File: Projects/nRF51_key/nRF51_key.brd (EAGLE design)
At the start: 45.7 x 12 mm, 14 parts, among them IC1 FT230XQ, J1 47571-0001, X1 USBPCB

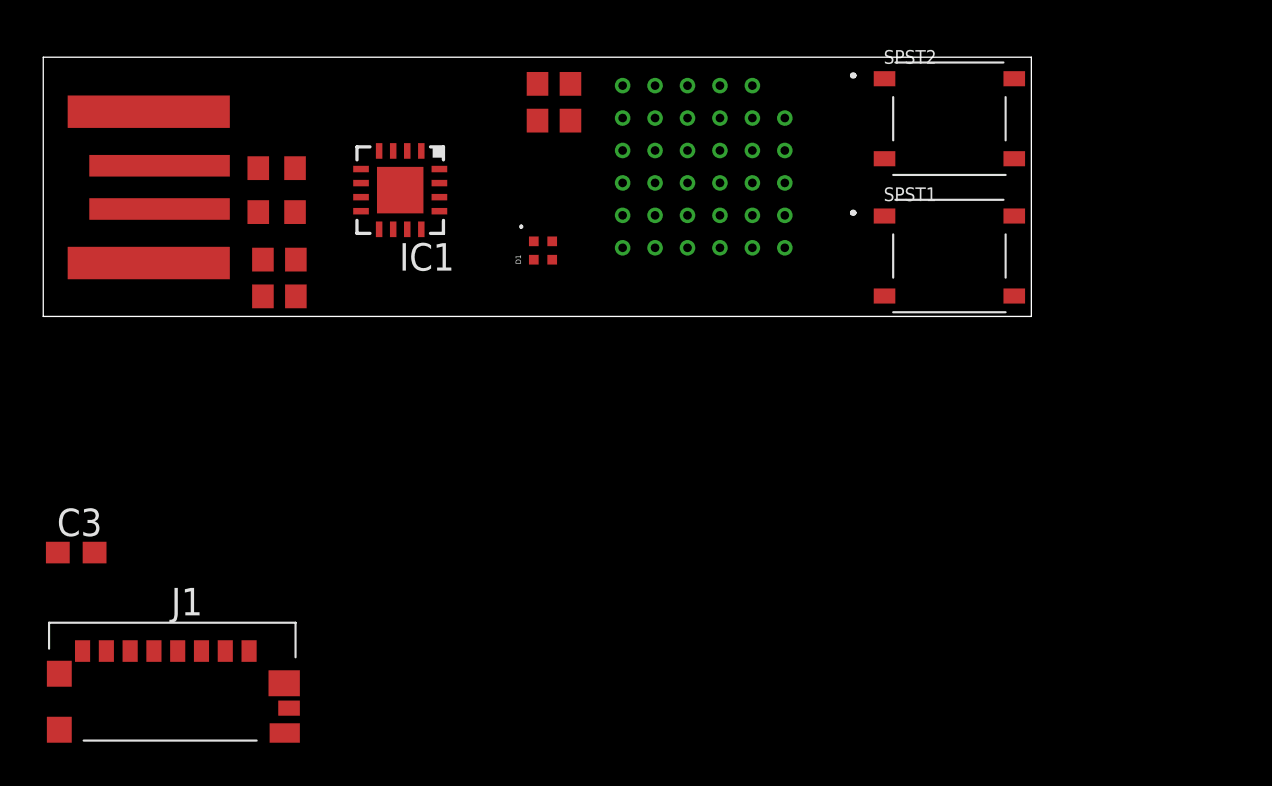
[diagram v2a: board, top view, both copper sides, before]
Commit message: Corrected SD card library
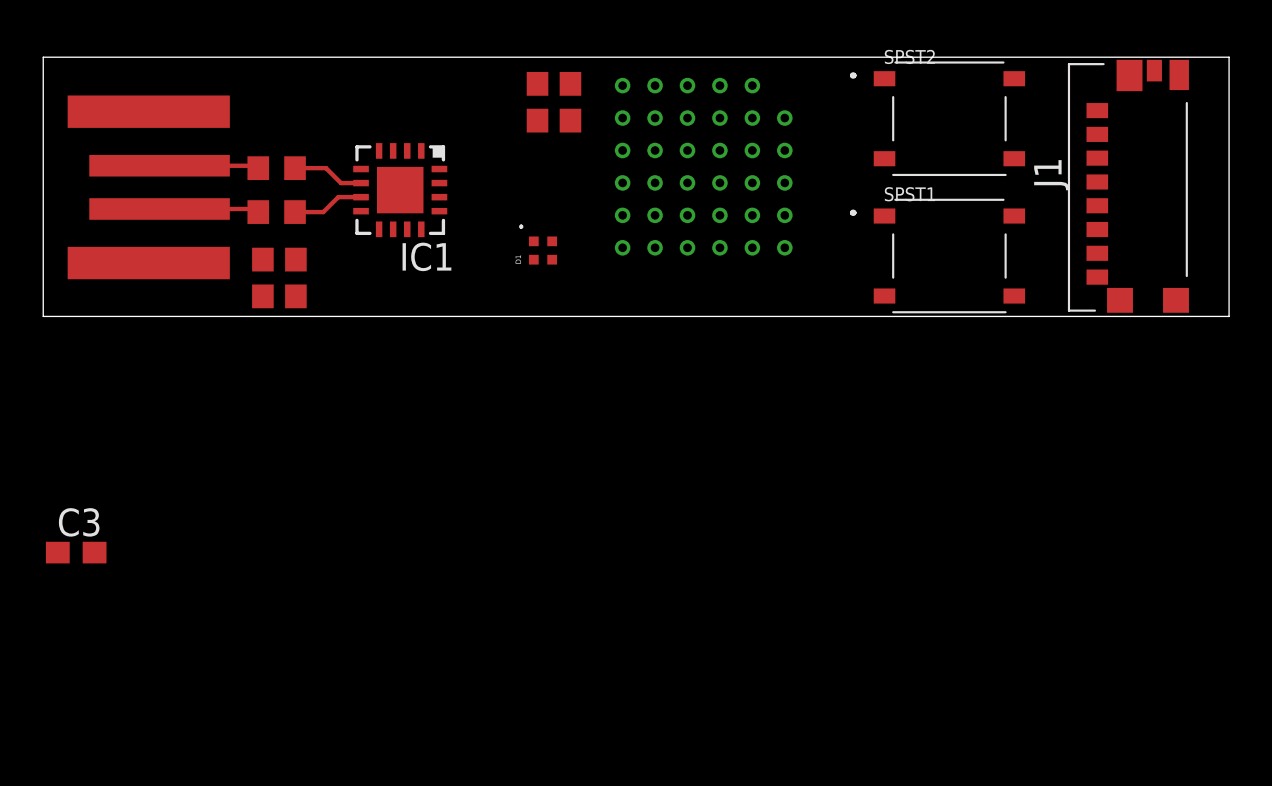
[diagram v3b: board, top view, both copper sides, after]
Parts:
- moved J1 49.8 mm to (50.2, 14.0), turned to 90 degrees
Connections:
- net CLK: now also J1.25; no longer J1.5
- net CS: now also J1.22; no longer J1.2
- net GND: now also J1.26; no longer J1.6
- net MISO: now also J1.27; no longer J1.7
- net MOSI: now also J1.23; no longer J1.3
- net SWDCLK: now also J1.21; no longer J1.8
- net SWDIO: now also J1.28; no longer J1.1
- net VDD: now also J1.24; no longer J1.4
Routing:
- net USBDM: track 0.00 -> 4.62 mm
- net USBDP: track 0.00 -> 4.61 mm
- net IC1_USBDM: track 0.00 -> 3.34 mm
- net IC1_USBDP: track 0.00 -> 3.34 mm
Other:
- board size 45.7 x 12 mm -> 54.8 x 12 mm
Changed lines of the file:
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@@
 <board>
 <plain>
-<wire x1="0" y1="8.001" x2="45.7" y2="8.001" width="0" layer="20"/>
-<wire x1="45.7" y1="8.001" x2="45.7" y2="19.99" width="0" layer="20"/>
-<wire x1="45.7" y1="19.99" x2="0" y2="19.99" width="0" layer="20"/>
+<wire x1="0" y1="8.001" x2="54.844" y2="8.001" width="0" layer="20"/>
+<wire x1="54.844" y1="8.001" x2="54.844" y2="19.99" width="0" layer="20"/>
+<wire x1="54.844" y1="19.99" x2="0" y2="19.99" width="0" layer="20"/>
 <wire x1="0" y1="19.99" x2="0" y2="8.001" width="0" layer="20"/>
 </plain>
@@
 <attribute name="VALUE" x="9.906" y="12.827" size="1.27" layer="27"/>
 </element>
-<element name="J1" library="SD_Card" package="47571-0001" value="47571-0001" x="5.969" y="-8.89" smashed="yes">
-<attribute name="NAME" x="6.645" y="-5.189" size="1.27" layer="25" align="center"/>
-<attribute name="VALUE" x="5.883" y="-12.555" size="1.27" layer="27" align="center"/>
+<element name="J1" library="SD_Card" package="47571-0001" value="47571-0001" x="50.165" y="13.97" smashed="yes" rot="R90">
+<attribute name="NAME" x="46.464" y="14.646" size="1.27" layer="25" rot="R90" align="center"/>
+<attribute name="VALUE" x="53.83" y="13.884" size="1.27" layer="27" rot="R90" align="center"/>
 </element>
 </elements>
@@
 <contactref element="C2" pad="2"/>
 <contactref element="C1" pad="2"/>
-<contactref element="J1" pad="6"/>
+<contactref element="J1" pad="26"/>
 <contactref element="J1" pad="13"/>
 <contactref element="J1" pad="11"/>
@@
 <contactref element="J1" pad="9"/>
 <contactref element="J1" pad="10"/>
+<wire x1="51.39" y1="19.37" x2="52.54" y2="19.17" width="0" layer="19" extent="1-1"/>
+<wire x1="50.24" y1="19.145" x2="51.39" y2="19.37" width="0" layer="19" extent="1-1"/>
+<wire x1="44.91" y1="15.295" x2="50.24" y2="19.145" width="0" layer="19" extent="1-1"/>
+<wire x1="48.75" y1="12.02" x2="44.91" y2="15.295" width="0" layer="19" extent="1-1"/>
+<wire x1="49.8" y1="8.745" x2="48.75" y2="12.02" width="0" layer="19" extent="1-1"/>
+<wire x1="52.39" y1="8.745" x2="49.8" y2="8.745" width="0" layer="19" extent="1-1"/>
+<wire x1="44.91" y1="8.945" x2="49.8" y2="8.745" width="0" layer="19" extent="1-1"/>
 <wire x1="38.91" y1="15.295" x2="44.91" y2="15.295" width="0" layer="19" extent="1-1"/>
-<wire x1="44.91" y1="8.945" x2="44.91" y2="15.295" width="0" layer="19" extent="1-1"/>
 <wire x1="38.91" y1="8.945" x2="44.91" y2="8.945" width="0" layer="19" extent="1-1"/>
 <wire x1="32.797" y1="18.676" x2="38.91" y2="15.295" width="0" layer="19" extent="1-1"/>
@@
 <wire x1="4.88" y1="17.47" x2="10.16" y2="8.929" width="0" layer="19" extent="1-1"/>
 <wire x1="2.374" y1="-2.921" x2="10.16" y2="8.929" width="0" layer="19" extent="1-1"/>
-<wire x1="0.744" y1="-8.525" x2="2.374" y2="-2.921" width="0" layer="19" extent="1-1"/>
-<wire x1="0.744" y1="-11.115" x2="0.744" y2="-8.525" width="0" layer="19" extent="1-1"/>
-<wire x1="7.319" y1="-7.475" x2="0.744" y2="-8.525" width="0" layer="19" extent="1-1"/>
-<wire x1="11.144" y1="-8.965" x2="7.319" y2="-7.475" width="0" layer="19" extent="1-1"/>
-<wire x1="11.369" y1="-10.115" x2="11.144" y2="-8.965" width="0" layer="19" extent="1-1"/>
-<wire x1="11.169" y1="-11.265" x2="11.369" y2="-10.115" width="0" layer="19" extent="1-1"/>
 </signal>
 <signal name="USBDP">
 <contactref element="X1" pad="USB_P"/>
 <contactref element="R2" pad="1"/>
-<wire x1="5.38" y1="14.97" x2="9.945" y2="14.859" width="0" layer="19" extent="1-1"/>
+<wire x1="5.38" y1="14.97" x2="9.834" y2="14.97" width="0.2032" layer="1"/>
+<wire x1="9.834" y1="14.97" x2="9.945" y2="14.859" width="0.2032" layer="1"/>
 </signal>
 <signal name="USBDM">
 <contactref element="X1" pad="USB_M"/>
 <contactref element="R1" pad="1"/>
-<wire x1="5.38" y1="12.97" x2="9.945" y2="12.827" width="0" layer="19" extent="1-1"/>
+<wire x1="5.38" y1="12.97" x2="9.802" y2="12.97" width="0.2032" layer="1"/>
+<wire x1="9.802" y1="12.97" x2="9.945" y2="12.827" width="0.2032" layer="1"/>
 </signal>
 <signal name="VBUS">
@@
 <contactref element="IC1" pad="9"/>
 <contactref element="IC1" pad="1"/>
-<contactref element="J1" pad="4"/>
-<wire x1="28.297" y1="15.676" x2="28.297" y2="17.176" width="0" layer="19" extent="1-1"/>
+<contactref element="J1" pad="24"/>
+<wire x1="28.297" y1="15.676" x2="48.75" y2="14.22" width="0" layer="19" extent="1-1"/>
+<wire x1="28.297" y1="17.176" x2="28.297" y2="15.676" width="0" layer="19" extent="1-1"/>
 <wire x1="26.797" y1="17.176" x2="28.297" y2="17.176" width="0" layer="19" extent="1-1"/>
 <wire x1="26.797" y1="15.676" x2="28.297" y2="15.676" width="0" layer="19" extent="1-1"/>
@@
 <wire x1="15.535" y1="12.0305" x2="14.6975" y2="12.868" width="0" layer="19" extent="1-1"/>
 <wire x1="22.689" y1="11.474" x2="22.86" y2="17.057" width="0" layer="19" extent="1-1"/>
-<wire x1="5.119" y1="-7.475" x2="15.535" y2="12.0305" width="0" layer="19" extent="1-1"/>
 </signal>
 <signal name="BTN1">
@@
 <contactref element="IC1" pad="7"/>
 <contactref element="R1" pad="2"/>
-<wire x1="11.645" y1="12.827" x2="14.6975" y2="13.518" width="0" layer="19" extent="1-1"/>
+<wire x1="11.645" y1="12.827" x2="12.954" y2="12.827" width="0.2032" layer="1"/>
+<wire x1="13.645" y1="13.518" x2="14.6975" y2="13.518" width="0.2032" layer="1"/>
+<wire x1="12.954" y1="12.827" x2="13.645" y2="13.518" width="0.2032" layer="1"/>
 </signal>
 <signal name="IC1_USBDP">
 <contactref element="IC1" pad="6"/>
 <contactref element="R2" pad="2"/>
-<wire x1="11.645" y1="14.859" x2="14.6975" y2="14.168" width="0" layer="19" extent="1-1"/>
+<wire x1="11.645" y1="14.859" x2="13.081" y2="14.859" width="0.2032" layer="1"/>
+<wire x1="13.772" y1="14.168" x2="14.6975" y2="14.168" width="0.2032" layer="1"/>
+<wire x1="13.081" y1="14.859" x2="13.772" y2="14.168" width="0.2032" layer="1"/>
 </signal>
 <signal name="MISO">
-<contactref element="J1" pad="7"/>
+<contactref element="J1" pad="27"/>
 </signal>
 <signal name="CLK">
-<contactref element="J1" pad="5"/>
+<contactref element="J1" pad="25"/>
 </signal>
 <signal name="MOSI">
-<contactref element="J1" pad="3"/>
+<contactref element="J1" pad="23"/>
 </signal>
 <signal name="CS">
-<contactref element="J1" pad="2"/>
+<contactref element="J1" pad="22"/>
 </signal>
 <signal name="SWDIO">
 <contactref element="U$1" pad="SWDIO"/>
-<contactref element="J1" pad="1"/>
-<wire x1="1.819" y1="-7.475" x2="34.297" y2="17.176" width="0" layer="19" extent="1-1"/>
+<contactref element="J1" pad="28"/>
+<wire x1="34.297" y1="17.176" x2="48.75" y2="9.82" width="0" layer="19" extent="1-1"/>
 </signal>
 <signal name="SWDCLK">
 <contactref element="U$1" pad="SWDCLK"/>
-<contactref element="J1" pad="8"/>
-<wire x1="9.519" y1="-7.475" x2="34.297" y2="15.676" width="0" layer="19" extent="1-1"/>
+<contactref element="J1" pad="21"/>
+<wire x1="34.297" y1="15.676" x2="48.75" y2="17.52" width="0" layer="19" extent="1-1"/>
 </signal>
 </signals>

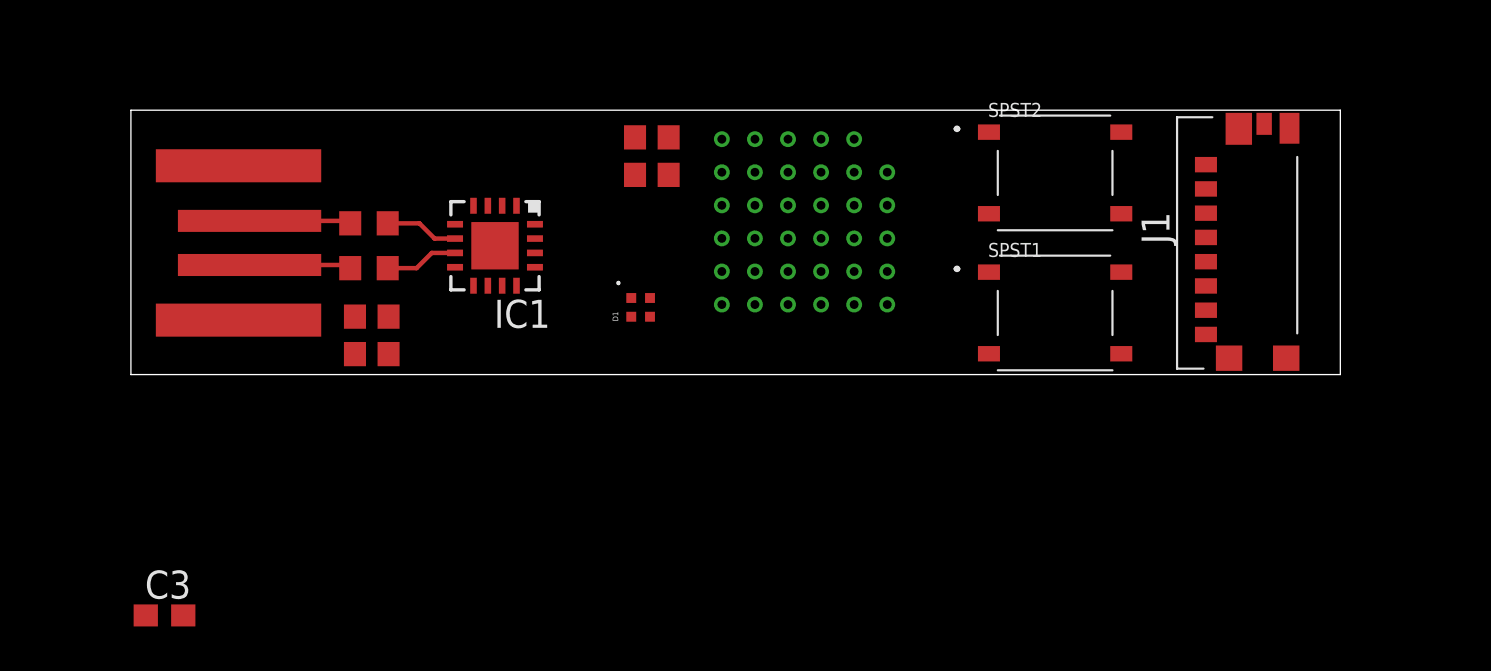
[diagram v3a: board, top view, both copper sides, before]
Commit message: Added buttons on ZLL Added pads on nRF51 key SD prog finished N5 lib updated
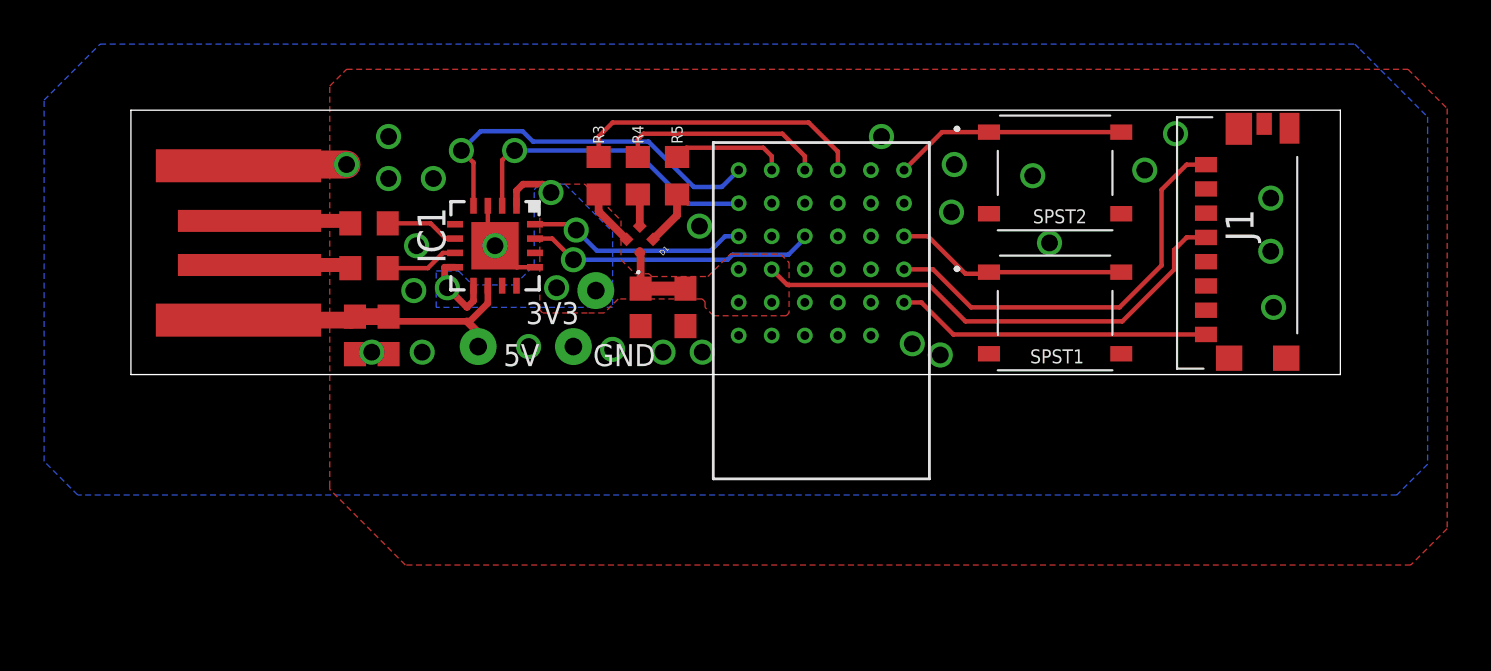
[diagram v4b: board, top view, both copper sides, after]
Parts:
- removed C3: (no value), Passives:C0603
- added R3, R4, R5: (no value), Passives:R0603
- added U$11, U$19, U$20: PAD, ParanoidStudio:PAD_0.8
- moved U$1 10.4 mm to (35.2, 17.3), turned to 180 degrees
- moved C5 7.23 mm to (25.1, 11.0), turned to 270 degrees
- moved C4 6.97 mm to (23.1, 11.0), turned to 270 degrees
- moved D1 3.09 mm to (23.1, 14.1), turned to 225 degrees
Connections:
- new net LEDB: R5.1, U$1.P002
- new net LEDG: R4.1, U$1.P001
- new net LEDR: R3.1, U$1.P003
- new net N$1: D1.2, R3.2
- new net N$2: D1.3, R4.2
- new net N$3: D1.4, R5.2
- net !CTS: now also U$1.P031
- net !RTS: now also U$1.P024
- net BTN1: now also U$1.P012
- net BTN2: now also U$1.P008
- net GND: now also U$20.PAD; no longer C3.2
- net RXD: now also U$1.P030
- net TXD: now also U$1.P023
- net VBUS: now also U$19.PAD
- net VDD: now also U$11.PAD
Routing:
- net VDD: track 0.00 -> 32.8 mm, vias 0 -> 3
- net SWDCLK: track 0.00 -> 19.1 mm
- net !CTS: track 0.00 -> 17.0 mm, vias 0 -> 1
- net SWDIO: track 0.00 -> 14.3 mm
- net RXD: track 0.00 -> 14.0 mm, vias 0 -> 1
- net VBUS: track 0.00 -> 14.0 mm
- net LEDR: track 0.00 -> 13.4 mm
- net TXD: track 0.00 -> 13.1 mm, vias 0 -> 1
- net BTN1: track 0.00 -> 10.6 mm
- net BTN2: track 0.00 -> 10.6 mm
- net !RTS: track 0.00 -> 10.1 mm, vias 0 -> 1
- net LEDG: track 0.00 -> 9.53 mm
- net GND: track 0.00 -> 9.09 mm, vias 0 -> 26
- net LEDB: track 0.00 -> 5.26 mm
- net N$1: track 0.00 -> 2.56 mm
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- added copper zone on layer 1, net GND
- added copper zone on layer 16, net GND
- added copper zone on layer 1, net VDD
- added copper zone on layer 16, net VDD
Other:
- board text added: "3V3"
- board text added: "5V"
- board text added: "GND"

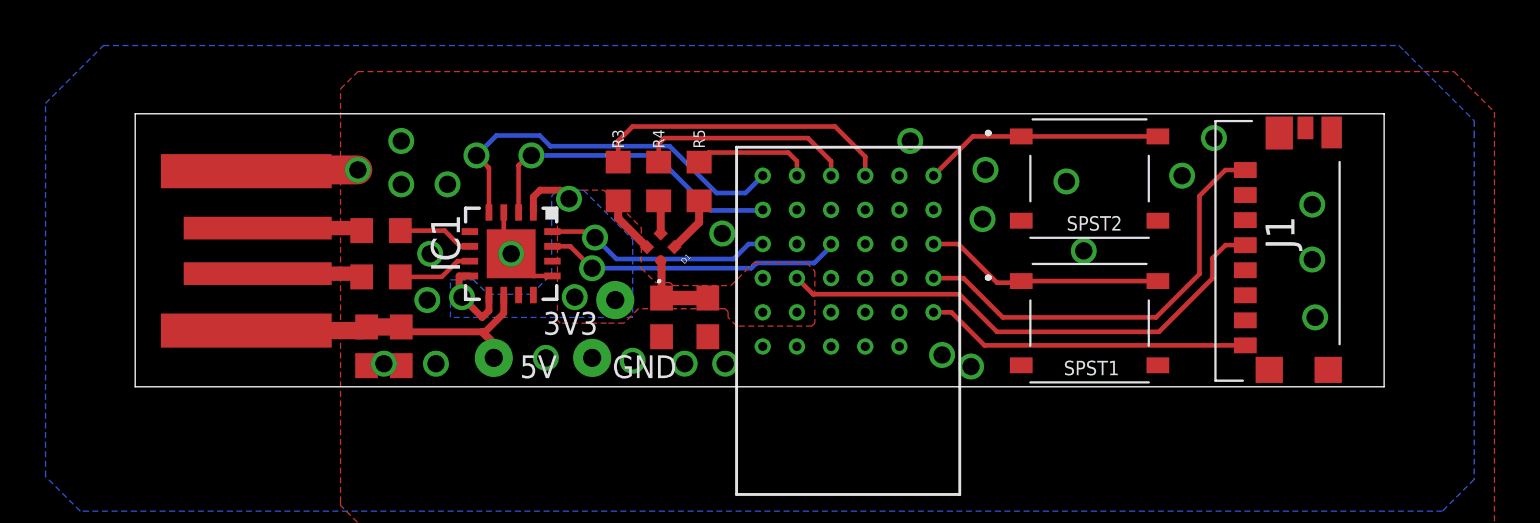
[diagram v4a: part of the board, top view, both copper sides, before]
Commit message: nRF51 dongle with new pins
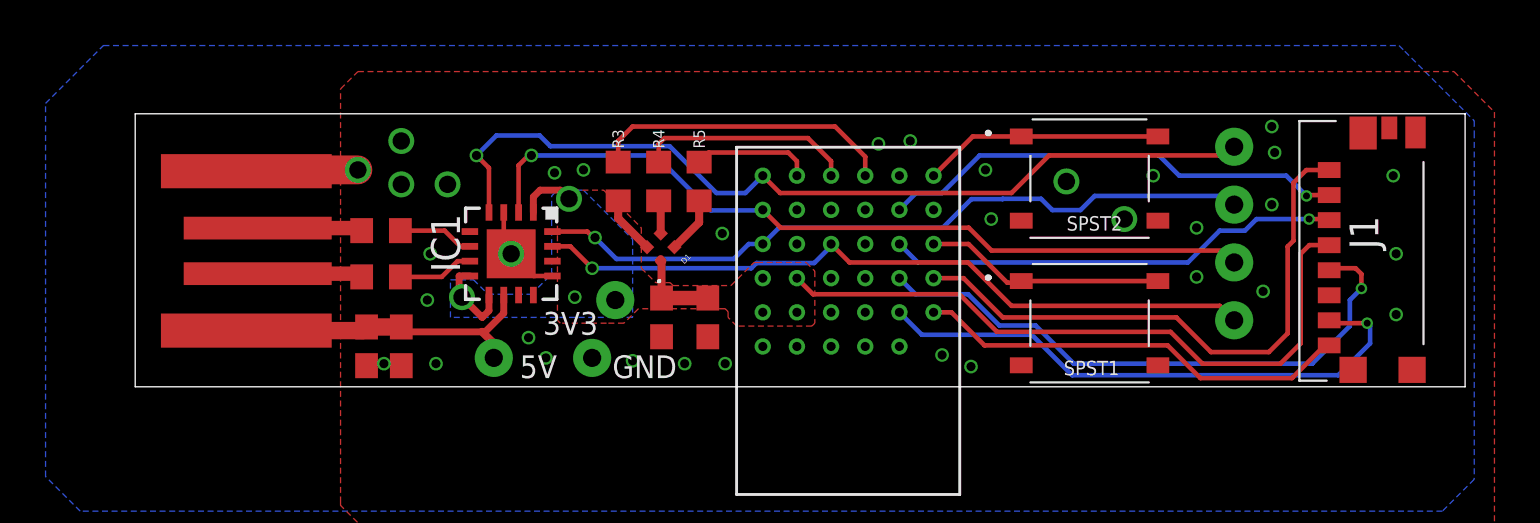
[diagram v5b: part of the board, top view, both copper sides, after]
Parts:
- added U$23, U$24, U$25, U$26: PAD, ParanoidStudio:PAD_0.8
- moved J1 3.68 mm to (53.8, 14.0)
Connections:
- net !CTS: now also U$26.PAD
- net !RTS: now also U$25.PAD
- net CLK: now also U$1.P013
- net CS: now also U$1.P011
- net MISO: now also U$1.P018
- net MOSI: now also U$1.P015
- net RXD: now also U$24.PAD
- net TXD: now also U$23.PAD
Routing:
- net CLK: track 0.00 -> 26.1 mm, vias 0 -> 1
- net MISO: track 0.00 -> 25.1 mm, vias 0 -> 1
- net !RTS: track 10.1 -> 32.3 mm
- net !CTS: track 17.0 -> 38.9 mm
- net RXD: track 14.0 -> 35.7 mm
- net CS: track 0.00 -> 20.6 mm, vias 0 -> 1
- net MOSI: track 0.00 -> 20.0 mm, vias 0 -> 1
- net TXD: track 13.1 -> 32.2 mm
- net SWDCLK: track 19.1 -> 25.8 mm
- net VDD: track 32.8 -> 39.4 mm
- net SWDIO: track 14.3 -> 19.2 mm
- net GND: vias 26 -> 35
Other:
- board size 54.8 x 12 mm -> 58.4 x 12 mm

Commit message: Order @ Boktech
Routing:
- net BTN2: track 10.6 -> 4.56 mm
- net BTN1: track 10.6 -> 4.58 mm
- net GND: track 9.09 -> 9.74 mm, vias 35 -> 44
- net !RTS: track 32.3 -> 31.7 mm
